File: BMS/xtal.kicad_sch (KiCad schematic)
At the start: 4 parts

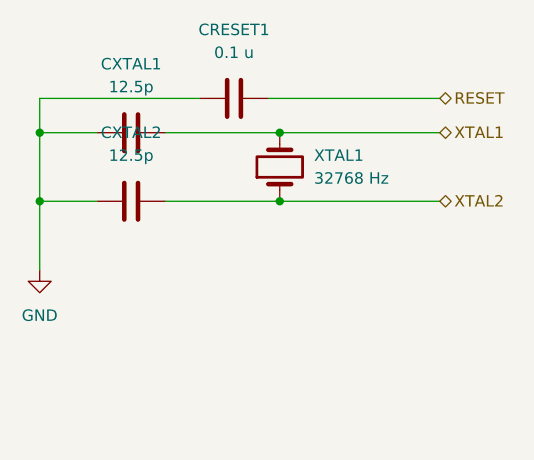
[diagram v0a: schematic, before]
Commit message: DCDC fix unavailable parts, BMS redesign, handle fix, rearrange top half
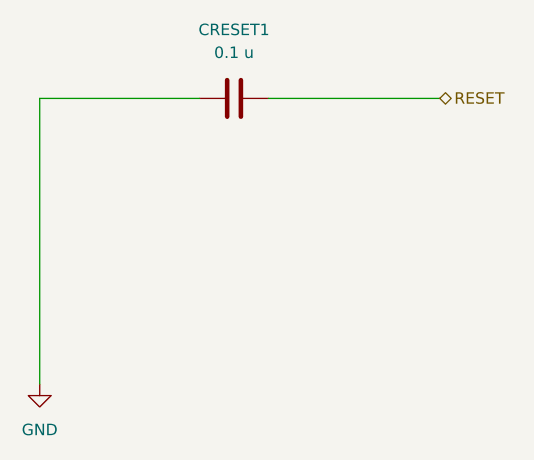
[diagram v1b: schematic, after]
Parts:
- removed CXTAL1, CXTAL2: 12.5p, symbol Device:C
- removed XTAL1: 32768 Hz, symbol Device:Crystal
- CRESET1: footprint (none) -> Capacitor_SMD:C_0603_1608Metric; Manufacturer_Part_Number (none) -> KAM15AR71H104KT
